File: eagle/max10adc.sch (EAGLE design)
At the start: 156 parts, among them IC1 MAX19506, IC2 MAX19506, J1 MOLEX_BNC_73100-0105, J2 MOLEX_BNC_73100-0105, J3 MOLEX_BNC_73100-0105, J4 MOLEX_BNC_73100-0105, U1 MAX4416ESA, U2 MAX4416ESA, U340G CH340G, Y1 ABL-12.000MHZ-B2

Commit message: some more stuff
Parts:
- RLED1, RLED2, RLED3, RLED4: value 220 -> 560; MPN MF-RES-0805-220 -> MF-RES-0805-560
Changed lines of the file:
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@@
 </part>
 <part name="GND25" library="supply1" deviceset="GND" device=""/>
-<part name="RLED1" library="resistor" deviceset="R-EU_" device="R0805" value="220">
+<part name="RLED1" library="resistor" deviceset="R-EU_" device="R0805" value="560">
 <attribute name="MF" value=""/>
-<attribute name="MPN" value="MF-RES-0805-220"/>
+<attribute name="MPN" value="MF-RES-0805-560"/>
 <attribute name="OC_NEWARK" value="unknown"/>
 </part>
@@
 </part>
 <part name="GND5" library="supply1" deviceset="GND" device=""/>
-<part name="RLED2" library="resistor" deviceset="R-EU_" device="R0805" value="220">
+<part name="RLED2" library="resistor" deviceset="R-EU_" device="R0805" value="560">
 <attribute name="MF" value=""/>
-<attribute name="MPN" value="MF-RES-0805-220"/>
+<attribute name="MPN" value="MF-RES-0805-560"/>
 <attribute name="OC_NEWARK" value="unknown"/>
 </part>
@@
 <attribute name="OC_NEWARK" value="unknown"/>
 </part>
-<part name="RLED3" library="resistor" deviceset="R-EU_" device="R0805" value="220">
+<part name="RLED3" library="resistor" deviceset="R-EU_" device="R0805" value="560">
 <attribute name="MF" value=""/>
-<attribute name="MPN" value="MF-RES-0805-220"/>
+<attribute name="MPN" value="MF-RES-0805-560"/>
 <attribute name="OC_NEWARK" value="unknown"/>
 </part>
@@
 <part name="GND8" library="supply1" deviceset="GND" device=""/>
 <part name="GND13" library="supply1" deviceset="GND" device=""/>
-<part name="RLED4" library="resistor" deviceset="R-EU_" device="R0805" value="220">
+<part name="RLED4" library="resistor" deviceset="R-EU_" device="R0805" value="560">
 <attribute name="MF" value=""/>
-<attribute name="MPN" value="MF-RES-0805-220"/>
+<attribute name="MPN" value="MF-RES-0805-560"/>
 <attribute name="OC_NEWARK" value="unknown"/>
 </part>

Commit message: some more stuff
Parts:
- removed AC_SW1, AC_SW2, AC_SW3, AC_SW4: 741G3157DBVR, 74xx-little-us:741G3157DBVR
- added ACR1, ACR2, ACR3, ACR4: 560, resistor:R-EU_R0805
- added K1, K2, K3, K4: AQY21SOP, relay:AQY21SOP
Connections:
- removed net N$14: AC_SW1G$1.A, C_AC1.2
- removed net N$17: AC_SW2G$1.B, CIN2.1, C_AC2.1, RIN2.1
- removed net N$20: AC_SW3G$1.B, CIN3.1, C_AC3.1, RIN3.1
- removed net N$22: AC_SW4G$1.B, CIN4.1, C_AC4.1, RIN4.1
- new net N$10: CIN1.1, C_AC1.1, K1.DS1, RIN1.1
- new net N$11: ACR1.2, K1.A
- new net N$32: ACR3.2, K3.A
- new net N$35: ACR4.2, K4.A
- net +3V3: no longer AC_SW1P.VCC, AC_SW2P.VCC, AC_SW3P.VCC, AC_SW4P.VCC
- net E_ACSW1: now also ACR1.1; no longer AC_SW1G$1.!A!/B
- net E_ACSW2: now also ACR2.1; no longer AC_SW2G$1.!A!/B
- net E_ACSW3: now also ACR3.1; no longer AC_SW3G$1.!A!/B
- net E_ACSW4: now also ACR4.1; no longer AC_SW4G$1.!A!/B
- net GND: now also K1.K, K2.K, K3.K, K4.K; no longer AC_SW1P.GND, AC_SW2P.GND, AC_SW3P.GND, AC_SW4P.GND
- net INJ1: now also C_AC1.2, K1.DS2; no longer AC_SW1G$1.X
- net INJ2: now also C_AC2.2, K2.DS2; no longer AC_SW2G$1.X
- net INJ3: now also C_AC3.2, K3.DS2; no longer AC_SW3G$1.X
- net INJ4: now also C_AC4.2, K4.DS2; no longer AC_SW4G$1.X
- net N$15: now also CIN2.1, C_AC2.1, K2.DS1, RIN2.1; no longer AC_SW1G$1.B, CIN1.1, C_AC1.1, RIN1.1
- net N$16: now also CIN3.1, C_AC3.1, K3.DS1, RIN3.1; no longer AC_SW2G$1.A, C_AC2.2
- net N$19: now also CIN4.1, C_AC4.1, K4.DS1, RIN4.1; no longer AC_SW3G$1.A, C_AC3.2
- net N$21: now also ACR2.2, K2.A; no longer AC_SW4G$1.A, C_AC4.2
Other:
- moved on the sheet: C_AC1, C_AC2, C_AC3, C_AC4

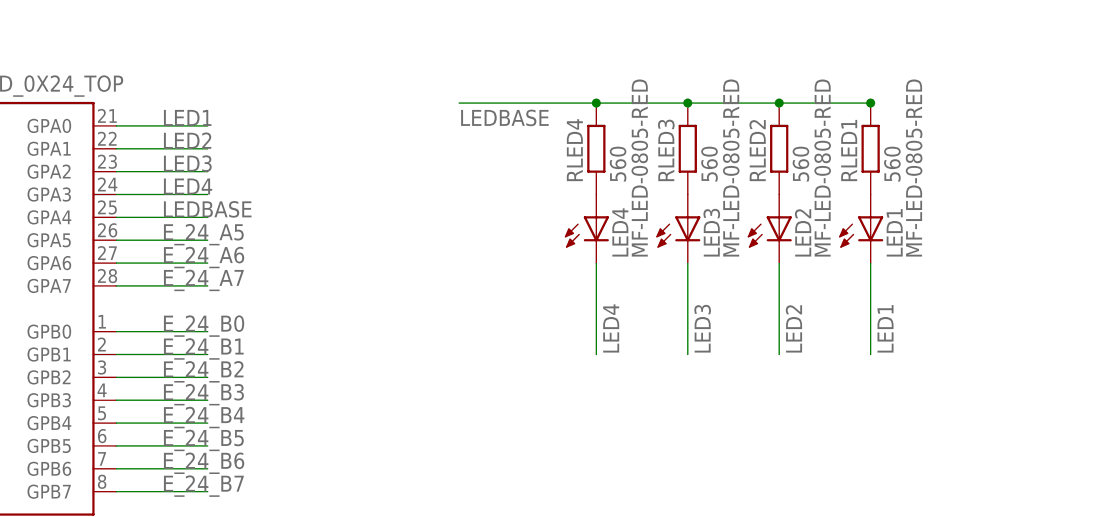
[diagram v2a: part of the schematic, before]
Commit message: routing of 8.6
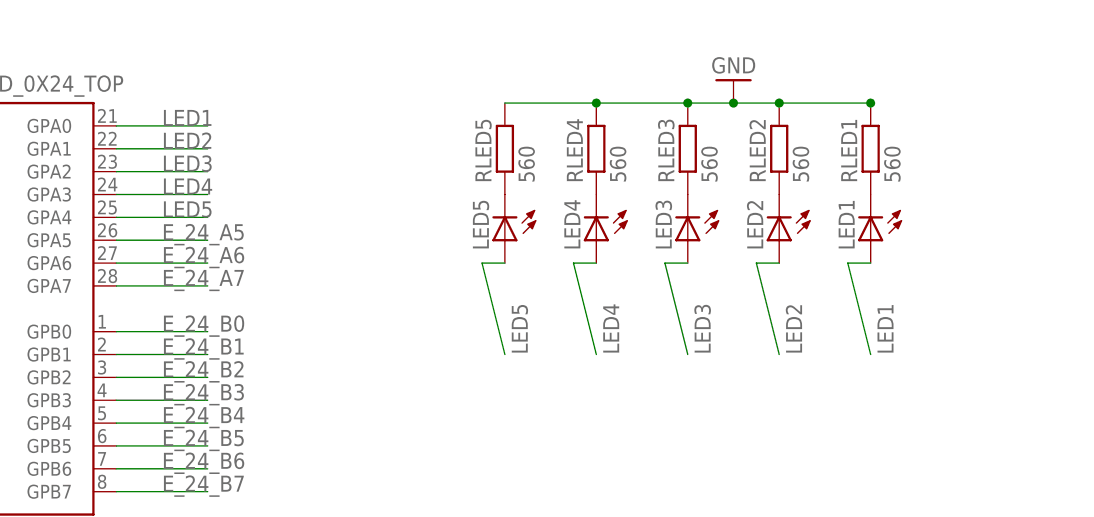
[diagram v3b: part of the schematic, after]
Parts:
- added LED5: MF-LED-0805-RED, led:LEDSML0805
- added RLED5: 560, resistor:R-EU_R0805
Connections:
- removed net LEDBASE: IOEXPAND_0X24_TOP.GPA4, RLED1.2, RLED2.2, RLED3.2, RLED4.2
- removed net N$34: LED1.A, RLED1.1
- removed net N$95: LED2.A, RLED2.1
- removed net N$97: LED3.A, RLED3.1
- new net LED5: IOEXPAND_0X24_TOP.GPA4, LED5.A
- new net N$12: LED3.C, RLED3.1
- new net N$13: LED2.C, RLED2.1
- new net N$14: LED1.C, RLED1.1
- new net N$17: LED5.C, RLED5.1
- net GND: now also RLED1.2, RLED2.2, RLED3.2, RLED4.2, RLED5.2
- net LED1: now also LED1.A; no longer LED1.C
- net LED2: now also LED2.A; no longer LED2.C
- net LED3: now also LED3.A; no longer LED3.C
- net LED4: now also LED4.A; no longer LED4.C
- net N$1: now also LED4.C; no longer LED4.A
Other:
- moved on the sheet: LED1, LED2, LED3, LED4

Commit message: routing of 8.6
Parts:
- CIN1, CIN2, CIN3, CIN4: MFN (none) -> MF-CAP-0603-10pF
- C_5V_10NF, C_AC1, C_AC2, C_AC3, C_AC4, C_OSC: MFN (none) -> MF-CAP-0603-0.01uF
- C_OSC1, C_OSC2: MFN (none) -> MF-CAP-0603-22pF
- DAC1: MFN (none) -> MCP4728-E/UN
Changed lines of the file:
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@@
 <part name="GND16" library="supply1" deviceset="GND" device=""/>
 <part name="+3V2" library="supply1" deviceset="+3V3" device=""/>
-<part name="C_OSC" library="rcl@1" deviceset="C-US" device="C0603" value="0.01uF"/>
+<part name="C_OSC" library="rcl@1" deviceset="C-US" device="C0603" value="0.01uF">
+<attribute name="MFN" value="MF-CAP-0603-0.01uF"/>
+</part>
 <part name="+3V4" library="supply1" deviceset="+3V3" device=""/>
 <part name="CV11" library="rcl" deviceset="C-EU" device="C0805K" value="0.1uF">
@@
 <part name="GND55" library="supply1" deviceset="GND" device=""/>
 <part name="+3V21" library="supply1" deviceset="+3V3" device=""/>
-<part name="C_AC1" library="rcl@1" deviceset="C-US" device="C0603" value="0.01uF"/>
+<part name="C_AC1" library="rcl@1" deviceset="C-US" device="C0603" value="0.01uF">
+<attribute name="MFN" value="MF-CAP-0603-0.01uF"/>
+</part>
 <part name="GND34" library="supply1" deviceset="GND" device=""/>
 <part name="IOEXPAND_0X20_BOT" library="microchip" deviceset="MCP23017" device="SS"/>
@@
 <part name="U340G" library="usb-serial" deviceset="CH340G" device=""/>
 <part name="Y1" library="SparkFun-FreqCtrl" deviceset="CRYSTAL" device="HC49US" value="ABL-12.000MHZ-B2"/>
-<part name="C_OSC1" library="rcl@1" deviceset="C-US" device="C0603" value="22pF"/>
-<part name="C_OSC2" library="rcl@1" deviceset="C-US" device="C0603" value="22pF"/>
+<part name="C_OSC1" library="rcl@1" deviceset="C-US" device="C0603" value="22pF">
+<attribute name="MFN" value="MF-CAP-0603-22pF"/>
+</part>
+<part name="C_OSC2" library="rcl@1" deviceset="C-US" device="C0603" value="22pF">
+<attribute name="MFN" value="MF-CAP-0603-22pF"/>
+</part>
 <part name="GND66" library="supply1" deviceset="GND" device=""/>
 <part name="+3V30" library="supply1" deviceset="+3V3" device=""/>
 <part name="GND67" library="supply1" deviceset="GND" device=""/>
-<part name="DAC1" library="Luca Eagle-Library" deviceset="MCP4728" device=""/>
+<part name="DAC1" library="Luca Eagle-Library" deviceset="MCP4728" device="">
+<attribute name="MFN" value="MCP4728-E/UN"/>
+</part>
 <part name="GND39" library="supply1" deviceset="GND" device=""/>
 <part name="GND43" library="supply1" deviceset="GND" device=""/>
@@
 <attribute name="MPN" value="BK0603HS330-T"/>
 </part>
-<part name="C_5V_10NF" library="rcl@1" deviceset="C-US" device="C0603" value="0.01uF"/>
+<part name="C_5V_10NF" library="rcl@1" deviceset="C-US" device="C0603" value="0.01uF">
+<attribute name="MFN" value="MF-CAP-0603-0.01uF"/>
+</part>
 <part name="GND45" library="supply1" deviceset="GND" device=""/>
-<part name="CIN1" library="rcl@1" deviceset="C-US" device="C0603" value="10pF"/>
-<part name="CIN2" library="rcl@1" deviceset="C-US" device="C0603" value="10pF"/>
-<part name="CIN3" library="rcl@1" deviceset="C-US" device="C0603" value="10pF"/>
-<part name="CIN4" library="rcl@1" deviceset="C-US" device="C0603" value="10pF"/>
+<part name="CIN1" library="rcl@1" deviceset="C-US" device="C0603" value="10pF">
+<attribute name="MFN" value="MF-CAP-0603-10pF"/>
+</part>
+<part name="CIN2" library="rcl@1" deviceset="C-US" device="C0603" value="10pF">
+<attribute name="MFN" value="MF-CAP-0603-10pF"/>
+</part>
+<part name="CIN3" library="rcl@1" deviceset="C-US" device="C0603" value="10pF">
+<attribute name="MFN" value="MF-CAP-0603-10pF"/>
+</part>
+<part name="CIN4" library="rcl@1" deviceset="C-US" device="C0603" value="10pF">
+<attribute name="MFN" value="MF-CAP-0603-10pF"/>
+</part>
 <part name="CGAIN2_1" library="rcl@1" deviceset="C-US" device="C0603" value="5pF">
 <attribute name="MPN" value="C1608C0G1H050C080AA"/>
@@
 <attribute name="MPN" value="AQY210S"/>
 </part>
-<part name="C_AC2" library="rcl@1" deviceset="C-US" device="C0603" value="0.01uF"/>
+<part name="C_AC2" library="rcl@1" deviceset="C-US" device="C0603" value="0.01uF">
+<attribute name="MFN" value="MF-CAP-0603-0.01uF"/>
+</part>
 <part name="GND35" library="supply1" deviceset="GND" device=""/>
 <part name="K2" library="relay" library_urn="urn:adsk.eagle:library:339" deviceset="AQY*" device="SOP" package3d_urn="urn:adsk.eagle:package:24376/1" technology="21">
 <attribute name="MPN" value="AQY210S"/>
 </part>
-<part name="C_AC3" library="rcl@1" deviceset="C-US" device="C0603" value="0.01uF"/>
+<part name="C_AC3" library="rcl@1" deviceset="C-US" device="C0603" value="0.01uF">
+<attribute name="MFN" value="MF-CAP-0603-0.01uF"/>
+</part>
 <part name="GND56" library="supply1" deviceset="GND" device=""/>
 <part name="K3" library="relay" library_urn="urn:adsk.eagle:library:339" deviceset="AQY*" device="SOP" package3d_urn="urn:adsk.eagle:package:24376/1" technology="21">
 <attribute name="MPN" value="AQY210S"/>
 </part>
-<part name="C_AC4" library="rcl@1" deviceset="C-US" device="C0603" value="0.01uF"/>
+<part name="C_AC4" library="rcl@1" deviceset="C-US" device="C0603" value="0.01uF">
+<attribute name="MFN" value="MF-CAP-0603-0.01uF"/>
+</part>
 <part name="GND57" library="supply1" deviceset="GND" device=""/>
 <part name="K4" library="relay" library_urn="urn:adsk.eagle:library:339" deviceset="AQY*" device="SOP" package3d_urn="urn:adsk.eagle:package:24376/1" technology="21">
@@
 <instance part="C_OSC" gate="G$1" x="-561.34" y="-22.86" smashed="yes">
 <attribute name="NAME" x="-565.15" y="-21.59" size="1.27" layer="95" ratio="10"/>
+<attribute name="MFN" x="-561.34" y="-22.86" size="1.778" layer="96" display="off"/>
 </instance>
 <instance part="+3V4" gate="G$1" x="-287.02" y="63.5"/>
@@
 <instance part="C_AC1" gate="G$1" x="-242.57" y="-106.68" smashed="yes" rot="R180">
 <attribute name="NAME" x="-238.76" y="-107.95" size="1.27" layer="95" ratio="10" rot="R180"/>
+<attribute name="MFN" x="-242.57" y="-106.68" size="1.778" layer="96" rot="R180" display="off"/>
 </instance>
 <instance part="GND34" gate="1" x="-218.44" y="-96.52" rot="R180"/>
@@
 <instance part="C_OSC1" gate="G$1" x="-447.04" y="-172.72" smashed="yes">
 <attribute name="NAME" x="-450.85" y="-171.45" size="1.27" layer="95" ratio="10"/>
+<attribute name="MFN" x="-447.04" y="-172.72" size="1.778" layer="96" display="off"/>
 </instance>
 <instance part="C_OSC2" gate="G$1" x="-439.42" y="-172.72" smashed="yes">
 <attribute name="NAME" x="-443.23" y="-171.45" size="1.27" layer="95" ratio="10"/>
+<attribute name="MFN" x="-439.42" y="-172.72" size="1.778" layer="96" display="off"/>
 </instance>
 <instance part="GND66" gate="1" x="-447.04" y="-187.96"/>
@@
 </instance>
 <instance part="GND67" gate="1" x="-419.1" y="-139.7" rot="R180"/>
-<instance part="DAC1" gate="G$1" x="-538.48" y="-144.78"/>
+<instance part="DAC1" gate="G$1" x="-538.48" y="-144.78">
+<attribute name="MFN" x="-538.48" y="-144.78" size="1.778" layer="96" display="off"/>
+</instance>
 <instance part="GND39" gate="1" x="-520.7" y="-137.16" rot="R180"/>
 <instance part="GND43" gate="1" x="-561.34" y="-147.32" rot="R270"/>
@@
 <instance part="C_5V_10NF" gate="G$1" x="-337.82" y="-132.08" smashed="yes">
 <attribute name="NAME" x="-334.01" y="-138.43" size="1.27" layer="95" ratio="10" rot="R90"/>
+<attribute name="MFN" x="-337.82" y="-132.08" size="1.778" layer="96" display="off"/>
 </instance>
 <instance part="GND45" gate="1" x="-337.82" y="-142.24"/>
 <instance part="CIN1" gate="G$1" x="-227.33" y="-124.46" smashed="yes">
 <attribute name="NAME" x="-231.14" y="-123.19" size="1.27" layer="95" ratio="10"/>
+<attribute name="MFN" x="-227.33" y="-124.46" size="1.778" layer="96" display="off"/>
 </instance>
 <instance part="CIN2" gate="G$1" x="-194.31" y="-124.46" smashed="yes">
 <attribute name="NAME" x="-198.12" y="-123.19" size="1.27" layer="95" ratio="10"/>
+<attribute name="MFN" x="-194.31" y="-124.46" size="1.778" layer="96" display="off"/>
 </instance>
 <instance part="CIN3" gate="G$1" x="-161.29" y="-124.46" smashed="yes">
 <attribute name="NAME" x="-165.1" y="-123.19" size="1.27" layer="95" ratio="10"/>
+<attribute name="MFN" x="-161.29" y="-124.46" size="1.778" layer="96" display="off"/>
 </instance>
 <instance part="CIN4" gate="G$1" x="-130.81" y="-124.46" smashed="yes">
 <attribute name="NAME" x="-134.62" y="-123.19" size="1.27" layer="95" ratio="10"/>
+<attribute name="MFN" x="-130.81" y="-124.46" size="1.778" layer="96" display="off"/>
 </instance>
 <instance part="CGAIN2_1" gate="G$1" x="-320.04" y="-163.83" smashed="yes" rot="R90">
@@
 <instance part="C_AC2" gate="G$1" x="-209.55" y="-106.68" smashed="yes" rot="R180">
 <attribute name="NAME" x="-205.74" y="-107.95" size="1.27" layer="95" ratio="10" rot="R180"/>
+<attribute name="MFN" x="-209.55" y="-106.68" size="1.778" layer="96" rot="R180" display="off"/>
 </instance>
 <instance part="GND35" gate="1" x="-185.42" y="-96.52" rot="R180"/>
@@
 <instance part="C_AC3" gate="G$1" x="-176.53" y="-106.68" smashed="yes" rot="R180">
 <attribute name="NAME" x="-172.72" y="-107.95" size="1.27" layer="95" ratio="10" rot="R180"/>
+<attribute name="MFN" x="-176.53" y="-106.68" size="1.778" layer="96" rot="R180" display="off"/>
 </instance>
 <instance part="GND56" gate="1" x="-152.4" y="-96.52" rot="R180"/>
@@
 <instance part="C_AC4" gate="G$1" x="-146.05" y="-106.68" smashed="yes" rot="R180">
 <attribute name="NAME" x="-142.24" y="-107.95" size="1.27" layer="95" ratio="10" rot="R180"/>
+<attribute name="MFN" x="-146.05" y="-106.68" size="1.778" layer="96" rot="R180" display="off"/>
 </instance>
 <instance part="GND57" gate="1" x="-121.92" y="-96.52" rot="R180"/>

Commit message: for board 8
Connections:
- net L128 renamed L127
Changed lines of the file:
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@@
 </segment>
 </net>
-<net name="L128" class="0">
+<net name="L127" class="0">
 <segment>
 <pinref part="FPGA" gate="G$1" pin="IO8_127"/>

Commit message: 8.6 improvements
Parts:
- removed PIN_ANALOG, PIN_EXP_IO_1, PIN_EXP_IO_2, PIN_IO_2, PIN_PWRGND_AIN: MF-CON-2.54mm-01x08, Seeed-Connector -2016:DIP-BLACK-MALE-HEADER-VERT(8P-2.54)
- added K5, K6, K7, K8: AQY21SOP, relay:AQY21SOP
- added LED6, LED7, LED8: MF-LED-0805-RED, led:LEDSML0805
- added PIN_AIN_IO2_PWRGND, PIN_ANALOG_IOEXP: 15-91-2160, pinhead+:PINHD-2X8SMT
- added RIN1_10K, RIN2_10K, RIN3_10K, RIN4_10K: 10K, resistor:R-EU_R0805
- added RLED6, RLED7, RLED8: 560, resistor:R-EU_R0805
- REG: MPN IFX8117MEV33 -> LDL1117S33R
- RGAIN1_1, RGAIN1_2, RGAIN1_3, RGAIN1_4, RGAIN3_1, RGAIN3_2, RGAIN3_3, RGAIN3_4: MPN MF-RES-0805-100 -> MF-RES-0805-100k
- RGAIN2_1, RGAIN2_2, RGAIN2_3, RGAIN2_4, RGAIN4_1, RGAIN4_2, RGAIN4_3, RGAIN4_4: MPN MF-RES-0805-1K -> MF-RES-0805-1M
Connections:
- removed net E_20_A6: IOEXPAND_0X20_BOT.GPA6, PIN_EXP_IO_1.1
- removed net E_20_A7: IOEXPAND_0X20_BOT.GPA7, PIN_EXP_IO_1.2
- removed net E_20_B5: IOEXPAND_0X20_BOT.GPB5, PIN_EXP_IO_1.3
- removed net E_20_B6: IOEXPAND_0X20_BOT.GPB6, PIN_EXP_IO_1.4
- removed net E_24_A5: IOEXPAND_0X24_TOP.GPA5, PIN_EXP_IO_1.6
- removed net E_24_A6: IOEXPAND_0X24_TOP.GPA6, PIN_EXP_IO_1.7
- removed net E_24_A7: IOEXPAND_0X24_TOP.GPA7, PIN_EXP_IO_1.8
- new net E_HIGHGAIN1: IOEXPAND_0X20_BOT.GPA4, K5.A
- new net E_HIGHGAIN2: IOEXPAND_0X20_BOT.GPA5, K6.A
- new net E_HIGHGAIN3: IOEXPAND_0X20_BOT.GPA6, K7.A
- new net E_HIGHGAIN4: IOEXPAND_0X20_BOT.GPA7, K8.A
- new net LED6: IOEXPAND_0X24_TOP.GPA5, LED6.A
- new net LED7: IOEXPAND_0X24_TOP.GPA6, LED7.A
- new net LED8: IOEXPAND_0X24_TOP.GPA7, LED8.A
- new net N$20: K5.DS1, RIN1_10K.1
- new net N$22: LED8.C, RLED8.1
- new net N$38: K6.DS1, RIN2_10K.1
- new net N$39: CIN3.1, C_AC3.1, K3.DS1, K7.DS2, RIN3.1
- new net N$40: K7.DS1, RIN3_10K.1
- new net N$41: CIN4.1, C_AC4.1, K4.DS1, K8.DS2, RIN4.1
- new net N$42: K8.DS1, RIN4_10K.1
- net +3V3: now also PIN_AIN_IO2_PWRGND.14, PIN_AIN_IO2_PWRGND.16; no longer PIN_PWRGND_AIN.1, PIN_PWRGND_AIN.2
- net +5V: now also PIN_AIN_IO2_PWRGND.10, PIN_AIN_IO2_PWRGND.12; no longer PIN_PWRGND_AIN.3, PIN_PWRGND_AIN.4
- net A10: now also PIN_ANALOG_IOEXP.8; no longer PIN_ANALOG.5
- net A11: now also PIN_ANALOG_IOEXP.10; no longer PIN_ANALOG.4
- net A12: now also PIN_ANALOG_IOEXP.12; no longer PIN_ANALOG.3
- net A13: now also PIN_ANALOG_IOEXP.14; no longer PIN_ANALOG.2
- net A14: now also PIN_ANALOG_IOEXP.16; no longer PIN_ANALOG.1
- net A6: now also PIN_ANALOG_IOEXP.2; no longer PIN_ANALOG.8
- net A7: now also PIN_ANALOG_IOEXP.4; no longer PIN_ANALOG.7
- net A8: now also PIN_ANALOG_IOEXP.6; no longer PIN_ANALOG.6
- net AIN1: now also PIN_AIN_IO2_PWRGND.1; no longer PIN_PWRGND_AIN.5
- net E_20_B7: now also PIN_AIN_IO2_PWRGND.2; no longer PIN_EXP_IO_1.5
- net E_24_B0: now also PIN_ANALOG_IOEXP.1; no longer PIN_EXP_IO_2.1
- net E_24_B1: now also PIN_ANALOG_IOEXP.3; no longer PIN_EXP_IO_2.2
- net E_24_B2: now also PIN_ANALOG_IOEXP.5; no longer PIN_EXP_IO_2.3
- net E_24_B3: now also PIN_ANALOG_IOEXP.7; no longer PIN_EXP_IO_2.4
- net E_24_B4: now also PIN_ANALOG_IOEXP.9; no longer PIN_EXP_IO_2.5
- net E_24_B5: now also PIN_ANALOG_IOEXP.11; no longer PIN_EXP_IO_2.6
- net E_24_B6: now also PIN_ANALOG_IOEXP.13; no longer PIN_EXP_IO_2.7
- net E_24_B7: now also PIN_ANALOG_IOEXP.15; no longer PIN_EXP_IO_2.8
- net E_OVSAMP1: now also IOEXPAND_0X20_BOT.GPB5; no longer IOEXPAND_0X20_BOT.GPA4
- net E_OVSAMP2: now also IOEXPAND_0X20_BOT.GPB6; no longer IOEXPAND_0X20_BOT.GPA5
- net GND: now also K5.K, K6.K, K7.K, K8.K, PIN_AIN_IO2_PWRGND.4, PIN_AIN_IO2_PWRGND.6, PIN_AIN_IO2_PWRGND.8, RLED6.2, RLED7.2, RLED8.2; no longer PIN_IO_2.1, PIN_PWRGND_AIN.6, PIN_PWRGND_AIN.7, PIN_PWRGND_AIN.8
- net INAMINUS1: now also RIN1_10K.2
- net INAMINUS2: now also RIN3_10K.2
- net INBMINUS1: now also RIN2_10K.2
- net INBMINUS2: now also RIN4_10K.2
- net IO_100: now also PIN_AIN_IO2_PWRGND.11; no longer PIN_IO_2.6
- net IO_101: now also PIN_AIN_IO2_PWRGND.13; no longer PIN_IO_2.7
- net IO_CLK_88: now also PIN_AIN_IO2_PWRGND.3; no longer PIN_IO_2.2
- net IO_CLK_89: now also PIN_AIN_IO2_PWRGND.5; no longer PIN_IO_2.3
- net IO_CLK_90: now also PIN_AIN_IO2_PWRGND.7; no longer PIN_IO_2.4
- net IO_CLK_91: now also PIN_AIN_IO2_PWRGND.9; no longer PIN_IO_2.5
- net L121: now also PIN_AIN_IO2_PWRGND.15; no longer PIN_IO_2.8
- net N$10: now also K5.DS2
- net N$15: now also K6.DS2
- net N$16: now also LED6.C, RLED6.1; no longer CIN3.1, C_AC3.1, K3.DS1, RIN3.1
- net N$19: now also LED7.C, RLED7.1; no longer CIN4.1, C_AC4.1, K4.DS1, RIN4.1
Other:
- moved on the sheet: CGAIN1_1, CGAIN1_2, CGAIN1_3, CGAIN1_4, CGAIN2_1, CGAIN2_2, CGAIN2_3, CGAIN2_4, CIN1, CIN2, CIN3, CIN4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
